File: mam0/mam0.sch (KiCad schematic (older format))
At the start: 14 parts

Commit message: готова схема, требуется проверка
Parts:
- removed C?: Конденсатор_керамический, N_RLC:Конденсатор_SMD_0603, symbol elements:Конденсатор_керамический
- removed DD?: LIS3DH, N_DD:акселерометр_LIS3DH, symbol elements:LIS3DH
- removed DD?: Память_eeprom_AT24C512C, N_DD:SO-8, symbol elements:Память_eeprom_AT24C512C
- removed R?: Резистор_0,065Вт, N_RLC:Резистор_SMD_0603_0,065_Вт, symbol elements:Резистор_0,065Вт
- added C? (x4): Конденсатор_керамический, N_RLC:Конденсатор_SMD_0603, symbol elements:Конденсатор_керамический
- added HL?: Светодиод, N_VD_HL:LED_D3.0mm, symbol elements:Светодиод
- added HL?: Светодиод, N_VD_HL:Светодиод_SMD_0603, symbol elements:Светодиод
- added R? (x4): Резистор_0,065Вт, N_RLC:Резистор_SMD_0603_0,065_Вт, symbol elements:Резистор_0,065Вт
- added VD?: Диод_шоттки, N_VD_HL:Диод_S13_SOD-123, symbol elements:Диод_шоттки
- added ZQ?: Резонатор_кварцевый, N_RLC:Резонатор_РК456МДУ(DIP), symbol elements:Резонатор_кварцевый
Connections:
- net 3V3_OUT: now also DD?.18 (AVCC), DD?.4 (VCC), DD?.6 (VCC), R?.1, VD?.2
- net GND_OUT: now also C?.2, DD?.21 (GND), DD?.3 (GND), DD?.5 (GND), G?.1 (GND), XP?.6 (GND), C?.2, C?.2, C?.2, C?.2, HL?.2, HL?.2, R?.2
- net MISO: now also DD?.16 (PB4(MISO)), XP?.1 (MISO)
- net MOSI: now also DD?.15 (PB3(MOSI/OC2)), XP?.4 (MOSI)
- net RESET: now also DD?.29 (PC6(RESET)), XP?.5 (RST)
- net SCL: now also DD?.28 (PC5(ADC5/SCL)), R?.2
- net SDA: now also DD?.27 (PC4(ADC4/SDA))
- net LED: now reaches DD?.1 (PD3(INT1))
- net LED: now also R?.1
- net RES_1: now reaches DD?.10 (PD6(AIN0))
- net RES_2: now reaches DD?.11 (PD7(AIN1))
- net MC_DOUT: now reaches DD?.13 (PB1(OC1A))
- net MC_DOUT: now also C?.1, G?.3 (3,2...6_В)
- net SCK: now reaches DD?.17 (PB5(SCK))
- net SCK: now also XP?.3 (SCK), R?.1
- net ADC_VCC: now reaches DD?.19 (ADC6)
- net ADC_VCC: now also R?.1, R?.2
- net at DD?.20 (AREF): now also C?.1
- net at DD?.7 (PB6(XTAL1/TOSC1)): now also C?.1, ZQ?.1
- net at DD?.8 (PB7(XTAL2/TOSC2)): now also C?.1, ZQ?.2
- net 3V_OUT: now reaches G?.2 (3В)
- net 3V_OUT: now also C?.1
- net at XP?.2 (VCC): now also VD?.1
- new net: HL?.1, HL?.1, R?.2
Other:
- note added: "не устанавливать в серию"
- moved on the sheet: C?, DD?, G?, R?, XP?

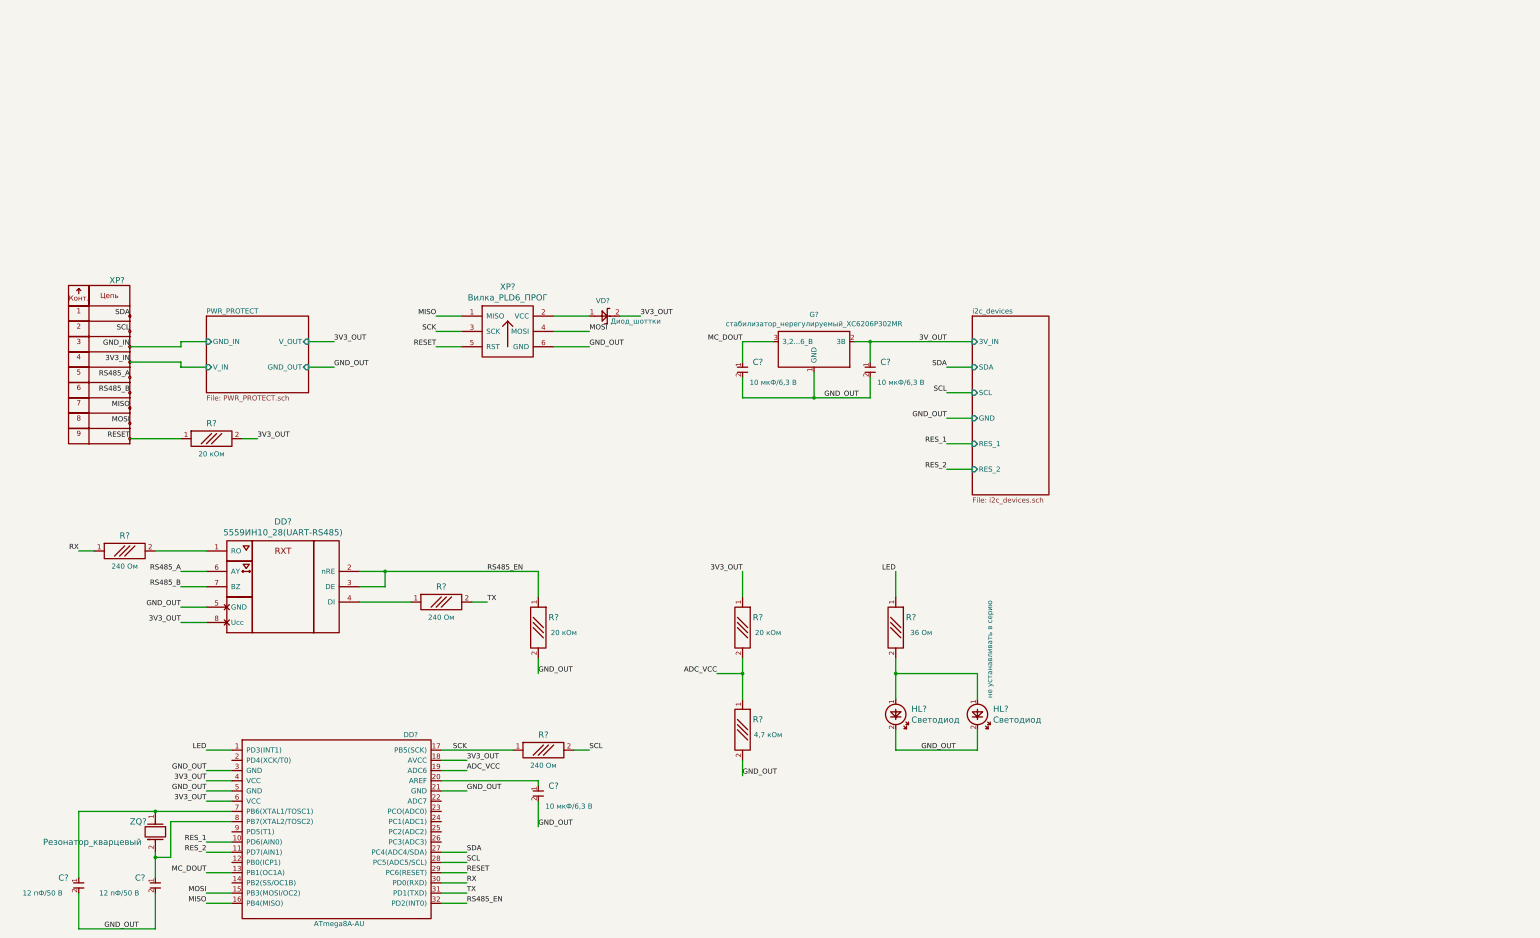
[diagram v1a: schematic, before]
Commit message: начата трассировка
сильно упрощенная схема
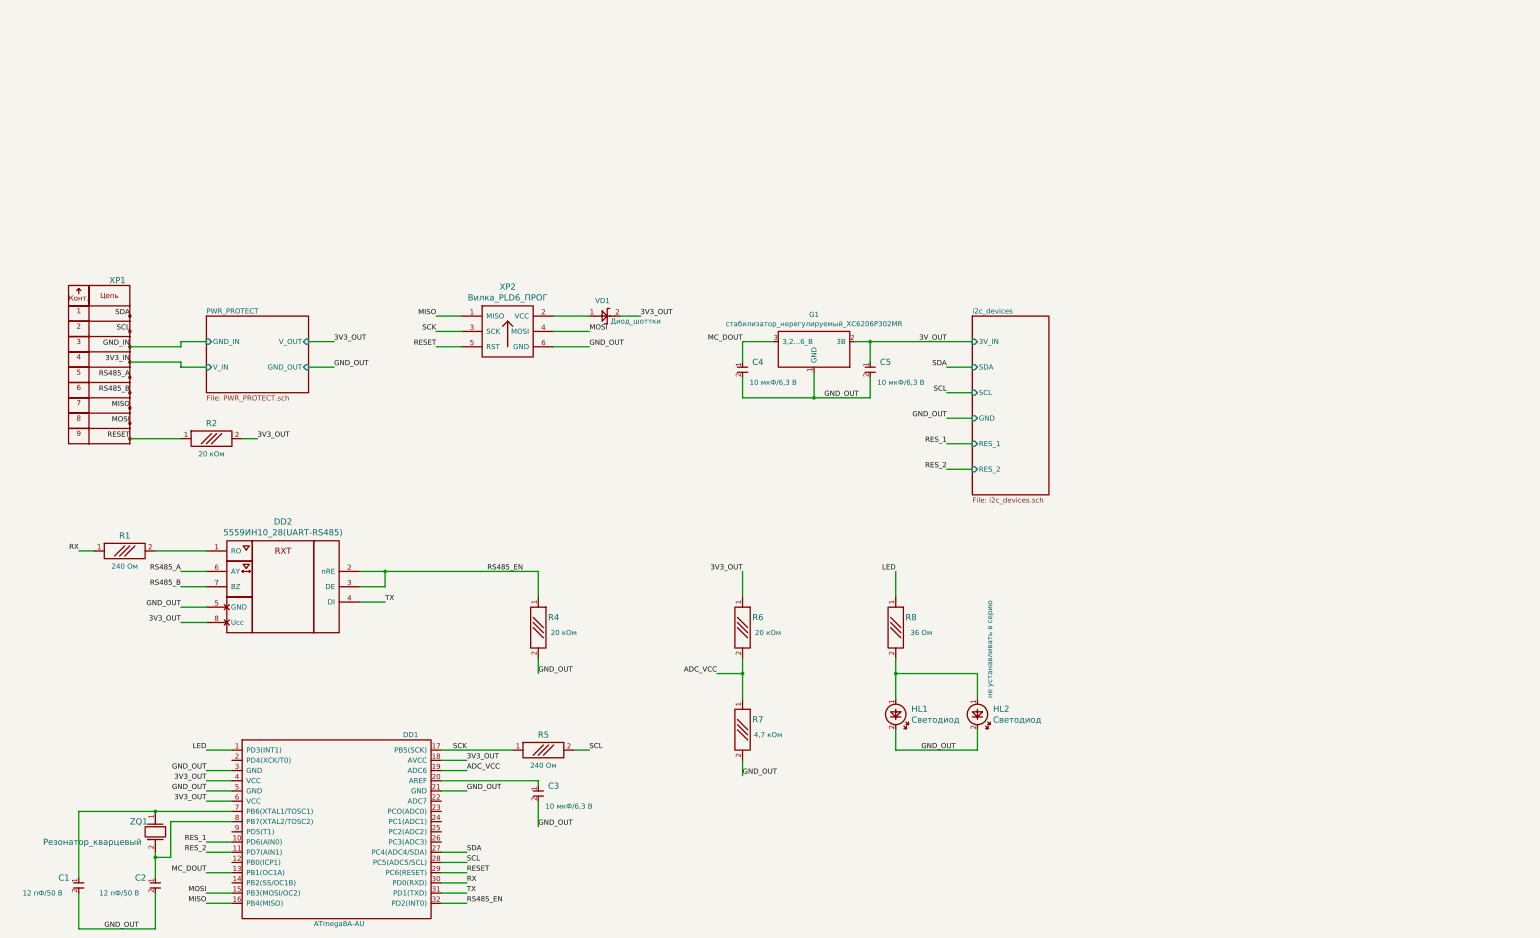
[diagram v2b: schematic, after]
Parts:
- removed R?: Резистор_0,065Вт, N_RLC:Резистор_SMD_0603_0,065_Вт, symbol elements:Резистор_0,065Вт
- gave numbers to parts that had none: 21
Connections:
- net TX: now also DD2.4 (DI)
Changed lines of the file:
@@
 $EndDescr
 $Comp
-L elements:ATmega8A-AU DD?
+L elements:ATmega8A-AU DD1
 U 1 1 5DB75FD0
 P 3100 5500
-F 0 "DD?" H 4750 5650 50  0000 C CNN
+F 0 "DD1" H 4750 5650 50  0000 C CNN
 F 1 "ATmega8A-AU" H 4050 3800 50  0000 C CNN
 F 2 "N_DD:микросхема_ATMEGA-8-161AU" H 3100 5500 50  0001 C CNN
@@
 $EndComp
 $Comp
-L elements:Конденсатор_керамический C?
+L elements:Конденсатор_керамический C4
 U 1 1 5DB7F015
 P 8000 1750
-F 0 "C?" V 7950 1900 60  0000 C CNN
+F 0 "C4" V 7950 1900 60  0000 C CNN
 F 1 "Конденсатор_керамический" H 8100 1650 60  0001 C CNN
 F 2 "N_RLC:Конденсатор_SMD_0603" H 8000 1750 60  0001 C CNN
@@
 $EndComp
 $Comp
-L elements:стабилизатор_нерегулируемый_XC6206P302MR G?
+L elements:стабилизатор_нерегулируемый_XC6206P302MR G1
 U 1 1 5DB818EA
 P 8350 1500
-F 0 "G?" H 8700 1765 50  0000 C CNN
+F 0 "G1" H 8700 1765 50  0000 C CNN
 F 1 "стабилизатор_нерегулируемый_XC6206P302MR" H 8700 1674 50  0000 C CNN
 F 2 "N_VD_HL:Транзистор_IRLML6344TR_SOT-23" H 8350 1500 50  0001 C CNN
@@
 $EndComp
 $Comp
-L elements:5559ИН10_28(UART-RS485) DD?
+L elements:5559ИН10_28(UART-RS485) DD2
 U 1 1 5DB83550
 P 3500 3900
-F 0 "DD?" H 3500 4537 60  0000 C CNN
+F 0 "DD2" H 3500 4537 60  0000 C CNN
 F 1 "5559ИН10_28(UART-RS485)" H 3500 4431 60  0000 C CNN
 F 2 "N_DD:SO-8" H 3500 3900 60  0001 C CNN
@@
 $EndComp
 $Comp
-L elements:Вилка_PLD6_ПРОГ XP?
+L elements:Вилка_PLD6_ПРОГ XP2
 U 1 1 5DB84AEB
 P 5700 1400
-F 0 "XP?" H 5700 1837 60  0000 C CNN
+F 0 "XP2" H 5700 1837 60  0000 C CNN
 F 1 "Вилка_PLD6_ПРОГ" H 5700 1731 60  0000 C CNN
 F 2 "N_X:Вилка_PLD6_вертикальная" H 5700 1400 60  0001 C CNN
@@
 $EndComp
 $Comp
-L elements:Вилка_х9 XP?
+L elements:Вилка_х9 XP1
 U 1 1 5DB8802C
 P 2000 1250
-F 0 "XP?" H 1800 1600 60  0000 L CNN
+F 0 "XP1" H 1800 1600 60  0000 L CNN
 F 1 "Вилка_х9" H 1750 -100 60  0001 C CNN
 F 2 "N_X:DSUB-DB9_End_Female" H 1425 1525 60  0001 C CNN
@@
 GND_OUT
 $Comp
-L elements:Резистор_0,065Вт R?
+L elements:Резистор_0,065Вт R2
 U 1 1 5DBA30D1
 P 2800 2450
-F 0 "R?" H 2800 2600 60  0000 C CNN
+F 0 "R2" H 2800 2600 60  0000 C CNN
 F 1 "Резистор_0,065Вт" H 2800 2300 60  0001 C CNN
 F 2 "N_RLC:Резистор_SMD_0603_0,065_Вт" H 2800 2450 60  0001 C CNN
@@
 Text Label 2500 4250 2    50   ~ 0
 3V3_OUT
-Text Label 1500 3550 2    50   ~ 0
-RX
-Text Label 5500 4050 0    50   ~ 0
+Text Label 4500 4050 0    50   ~ 0
 TX
 Wire Wire Line
-	4250 4050 4750 4050
-Wire Wire Line
 	4250 3750 4500 3750
 Wire Wire Line
@@
 	4500 3900 4250 3900
 $Comp
-L elements:Резистор_0,065Вт R?
-U 1 1 5DBB02D7
-P 1950 3550
-F 0 "R?" H 1950 3700 60  0000 C CNN
-F 1 "Резистор_0,065Вт" H 1950 3400 60  0001 C CNN
-F 2 "N_RLC:Резистор_SMD_0603_0,065_Вт" H 1950 3550 60  0001 C CNN
-F 3 "" H 1950 3550 60  0001 C CNN
-F 4 "R241" H 1950 3550 50  0001 C CNN "УГО"
-F 5 "240 Ом" H 1950 3400 50  0000 C CNN "Номинал"
-	1    1950 3550
-	1    0    0    -1
-$EndComp
-Wire Wire Line
-	1650 3550 1500 3550
-Wire Wire Line
-	2250 3550 2750 3550
-$Comp
-L elements:Резистор_0,065Вт R?
-U 1 1 5DBB1CAA
-P 5050 4050
-F 0 "R?" H 5050 4200 60  0000 C CNN
-F 1 "Резистор_0,065Вт" H 5050 3900 60  0001 C CNN
-F 2 "N_RLC:Резистор_SMD_0603_0,065_Вт" H 5050 4050 60  0001 C CNN
-F 3 "" H 5050 4050 60  0001 C CNN
-F 4 "R241" H 5050 4050 50  0001 C CNN "УГО"
-F 5 "240 Ом" H 5050 3900 50  0000 C CNN "Номинал"
-	1    5050 4050
-	1    0    0    -1
-$EndComp
-Wire Wire Line
-	5350 4050 5500 4050
-$Comp
-L elements:Резистор_0,065Вт R?
+L elements:Резистор_0,065Вт R4
 U 1 1 5DBB3372
 P 6000 4300
-F 0 "R?" V 5900 4450 60  0000 C CNN
+F 0 "R4" V 5900 4450 60  0000 C CNN
 F 1 "Резистор_0,065Вт" H 6000 4150 60  0001 C CNN
 F 2 "N_RLC:Резистор_SMD_0603_0,065_Вт" H 6000 4300 60  0001 C CNN
@@
 RS485_EN
 $Comp
-L elements:Резистор_0,065Вт R?
+L elements:Резистор_0,065Вт R5
 U 1 1 5DB95D43
 P 6050 5500
-F 0 "R?" H 6050 5650 60  0000 C CNN
+F 0 "R5" H 6050 5650 60  0000 C CNN
 F 1 "Резистор_0,065Вт" H 6050 5350 60  0001 C CNN
 F 2 "N_RLC:Резистор_SMD_0603_0,065_Вт" H 6050 5500 60  0001 C CNN
@@
 	6150 1400 6500 1400
 $Comp
-L elements:Диод_шоттки VD?
+L elements:Диод_шоттки VD1
 U 1 1 5DBA11EC
 P 6500 1250
-AR Path="/5DBA11EC" Ref="VD?"  Part="1"
+AR Path="/5DBA11EC" Ref="VD1"  Part="1"
 AR Path="/5DB9AA7C/5DBA11EC" Ref="VD?"  Part="1"
-F 0 "VD?" H 6700 1400 50  0000 R CNN
+F 0 "VD1" H 6700 1400 50  0000 R CNN
 F 1 "Диод_шоттки" H 7200 1200 50  0000 R CNN
 F 2 "N_VD_HL:Диод_S13_SOD-123" H 6400 1250 50  0001 C CNN
@@
 	5000 1550 5250 1550
 $Comp
-L elements:Конденсатор_керамический C?
+L elements:Конденсатор_керамический C5
 U 1 1 5DBAC76D
 P 9250 1750
-F 0 "C?" V 9200 1900 60  0000 C CNN
+F 0 "C5" V 9200 1900 60  0000 C CNN
 F 1 "Конденсатор_керамический" H 9350 1650 60  0001 C CNN
 F 2 "N_RLC:Конденсатор_SMD_0603" H 9250 1750 60  0001 C CNN
@@
 	5050 6700 5300 6700
 $Comp
-L elements:Резонатор_кварцевый ZQ?
+L elements:Резонатор_кварцевый ZQ1
 U 1 1 5DBB466E
 P 2250 6300
-F 0 "ZQ?" V 2150 6050 60  0000 L CNN
+F 0 "ZQ1" V 2150 6050 60  0000 L CNN
 F 1 "Резонатор_кварцевый" V 2350 5200 60  0000 L CNN
 F 2 "N_RLC:Резонатор_РК456МДУ(DIP)" H 2250 6300 60  0001 C CNN
@@
 	10250 2750 10000 2750
 $Comp
-L elements:Конденсатор_керамический C?
+L elements:Конденсатор_керамический C1
 U 1 1 5DC1361F
 P 1500 6800
-F 0 "C?" V 1450 6600 60  0000 L CNN
+F 0 "C1" V 1450 6600 60  0000 L CNN
 F 1 "Конденсатор_керамический" H 1600 6700 60  0001 C CNN
 F 2 "N_RLC:Конденсатор_SMD_0603" H 1500 6800 60  0001 C CNN
@@
 $EndComp
 $Comp
-L elements:Конденсатор_керамический C?
+L elements:Конденсатор_керамический C2
 U 1 1 5DC146FC
 P 2250 6800
-F 0 "C?" V 2200 6600 60  0000 L CNN
+F 0 "C2" V 2200 6600 60  0000 L CNN
 F 1 "Конденсатор_керамический" H 2350 6700 60  0001 C CNN
 F 2 "N_RLC:Конденсатор_SMD_0603" H 2250 6800 60  0001 C CNN
@@
 	3000 6900 2750 6900
 $Comp
-L elements:Конденсатор_керамический C?
+L elements:Конденсатор_керамический C3
 U 1 1 5DC1E99E
 P 6000 5900
-F 0 "C?" V 5950 6050 60  0000 C CNN
+F 0 "C3" V 5950 6050 60  0000 C CNN
 F 1 "Конденсатор_керамический" H 6100 5800 60  0001 C CNN
 F 2 "N_RLC:Конденсатор_SMD_0603" H 6000 5900 60  0001 C CNN
@@
 GND_OUT
 $Comp
-L elements:Резистор_0,065Вт R?
+L elements:Резистор_0,065Вт R6
 U 1 1 5DC35468
 P 8000 4300
-F 0 "R?" V 7900 4450 60  0000 C CNN
+F 0 "R6" V 7900 4450 60  0000 C CNN
 F 1 "Резистор_0,065Вт" H 8000 4150 60  0001 C CNN
 F 2 "N_RLC:Резистор_SMD_0603_0,065_Вт" H 8000 4300 60  0001 C CNN
@@
 $EndComp
 $Comp
-L elements:Резистор_0,065Вт R?
+L elements:Резистор_0,065Вт R7
 U 1 1 5DC375D4
 P 8000 5300
-F 0 "R?" V 7900 5450 60  0000 C CNN
+F 0 "R7" V 7900 5450 60  0000 C CNN
 F 1 "Резистор_0,065Вт" H 8000 5150 60  0001 C CNN
 F 2 "N_RLC:Резистор_SMD_0603_0,065_Вт" H 8000 5300 60  0001 C CNN
@@
 	3000 6500 2750 6500
 $Comp
-L elements:Резистор_0,065Вт R?
+L elements:Резистор_0,065Вт R8
 U 1 1 5DC50066
 P 9500 4300
-F 0 "R?" V 9400 4450 60  0000 C CNN
+F 0 "R8" V 9400 4450 60  0000 C CNN
 F 1 "Резистор_0,065Вт" H 9500 4150 60  0001 C CNN
 F 2 "N_RLC:Резистор_SMD_0603_0,065_Вт" H 9500 4300 60  0001 C CNN
@@
 	3000 5500 2750 5500
 $Comp
-L elements:Светодиод HL?
+L elements:Светодиод HL1
 U 1 1 5DC55A05
 P 9500 5000
-F 0 "HL?" V 9597 5153 60  0000 L CNN
+F 0 "HL1" V 9597 5153 60  0000 L CNN
 F 1 "Светодиод" V 9703 5153 60  0000 L CNN
 F 2 "N_VD_HL:LED_D3.0mm" H 9800 4500 60  0001 C CNN
@@
 $EndComp
 $Comp
-L elements:Светодиод HL?
+L elements:Светодиод HL2
 U 1 1 5DC57020
 P 10300 5000
-F 0 "HL?" V 10397 5153 60  0000 L CNN
+F 0 "HL2" V 10397 5153 60  0000 L CNN
 F 1 "Светодиод" V 10503 5153 60  0000 L CNN
 F 2 "N_VD_HL:Светодиод_SMD_0603" H 10600 4500 60  0001 C CNN
@@
 Text Notes 10450 5000 1    50   ~ 0
 не устанавливать в серию
+Wire Wire Line
+	4250 4050 4500 4050
+Text Label 1500 3550 2    50   ~ 0
+RX
+Wire Wire Line
+	2250 3550 2750 3550
+Wire Wire Line
+	1650 3550 1500 3550
+$Comp
+L elements:Резистор_0,065Вт R1
+U 1 1 5DBB02D7
+P 1950 3550
+F 0 "R1" H 1950 3700 60  0000 C CNN
+F 1 "Резистор_0,065Вт" H 1950 3400 60  0001 C CNN
+F 2 "N_RLC:Резистор_SMD_0603_0,065_Вт" H 1950 3550 60  0001 C CNN
+F 3 "" H 1950 3550 60  0001 C CNN
+F 4 "R241" H 1950 3550 50  0001 C CNN "УГО"
+F 5 "240 Ом" H 1950 3400 50  0000 C CNN "Номинал"
+	1    1950 3550
+	1    0    0    -1
+$EndComp
 $EndSCHEMATC
